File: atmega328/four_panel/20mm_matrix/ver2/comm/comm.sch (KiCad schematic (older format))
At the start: 11 parts, among them IC5 ATMEGA328-A, P1 CONN15, P2 CONN15, P4 CONN_2X2, P5 CONN_2X2, P6 CONN_2X2, P7 CONN_2X2, X5 CER_RESO

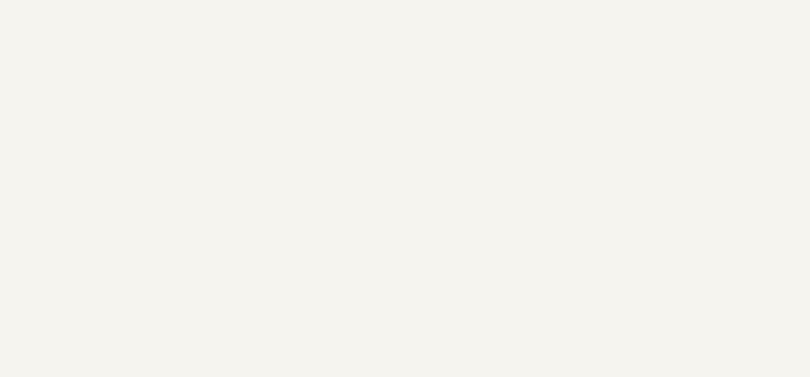
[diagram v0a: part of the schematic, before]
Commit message: Added ground pin header to backside of ver 2 com pcb.
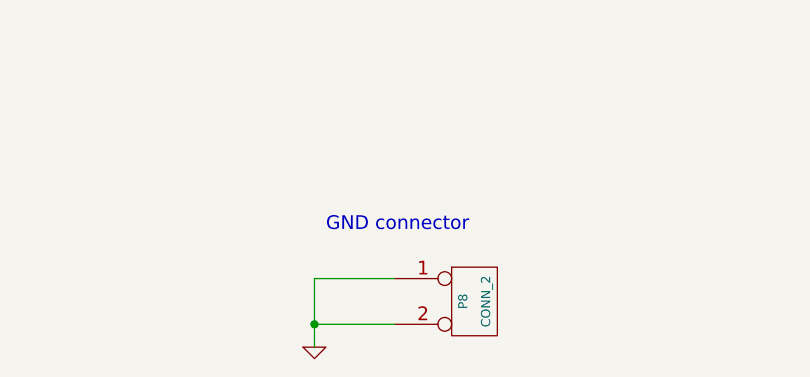
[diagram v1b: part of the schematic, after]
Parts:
- added P8: CONN_2, symbol CONN_2
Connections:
- net GND: now also P8.1 (P1), P8.2 (PM)
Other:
- note added: "GND connector"
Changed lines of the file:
@@
 NoConn ~ 14650 1650
 NoConn ~ 14650 2500
+$Comp
+L CONN_2 P8
+U 1 1 53C45937
+P 13050 5950
+F 0 "P8" V 13000 5950 40  0000 C CNN
+F 1 "CONN_2" V 13100 5950 40  0000 C CNN
+F 2 "" H 13050 5950 60  0000 C CNN
+F 3 "" H 13050 5950 60  0000 C CNN
+	1    13050 5950
+	1    0    0    -1
+$EndComp
+$Comp
+L GND #PWR019
+U 1 1 53C45946
+P 12350 6150
+F 0 "#PWR019" H 12350 6150 30  0001 C CNN
+F 1 "GND" H 12350 6080 30  0001 C CNN
+F 2 "" H 12350 6150 60  0000 C CNN
+F 3 "" H 12350 6150 60  0000 C CNN
+	1    12350 6150
+	1    0    0    -1
+$EndComp
+Wire Wire Line
+	12350 5850 12350 6150
+Wire Wire Line
+	12350 6050 12700 6050
+Wire Wire Line
+	12700 5850 12350 5850
+Connection ~ 12350 6050
+Text Notes 12400 5650 0    60   ~ 0
+GND connector
 $EndSCHEMATC

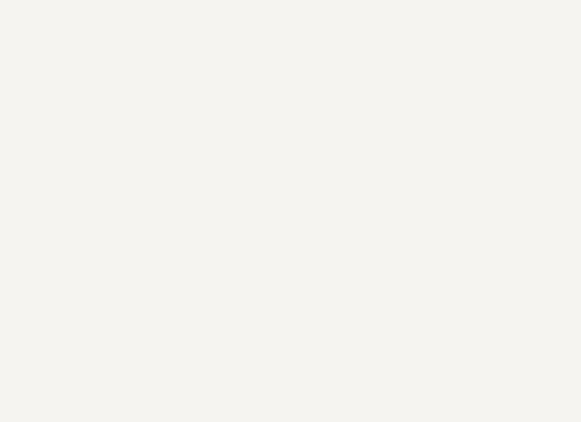
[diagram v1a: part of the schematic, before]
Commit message: Adde ground holes to 4x20mm atmega328 comm
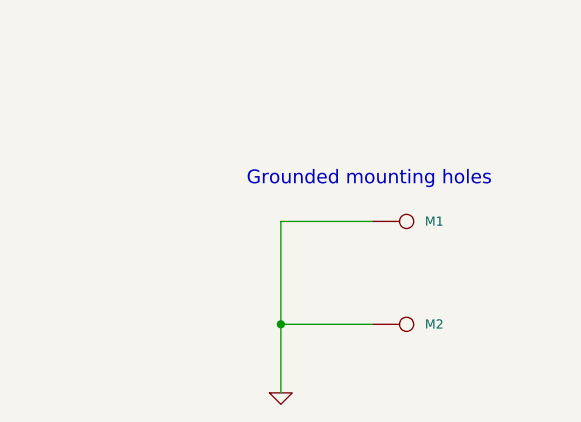
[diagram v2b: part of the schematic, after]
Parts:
- added M1, M2: CONN_1, symbol CONN_1
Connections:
- net GND: now also M1.1, M2.1
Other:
- note added: "Grounded mounting holes"
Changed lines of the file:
@@
 Text Notes 12400 5650 0    60   ~ 0
 GND connector
+$Comp
+L CONN_1 M1
+U 1 1 53CF2CE7
+P 15800 5650
+F 0 "M1" H 15880 5650 40  0000 L CNN
+F 1 "CONN_1" H 15800 5705 30  0001 C CNN
+F 2 "" H 15800 5650 60  0000 C CNN
+F 3 "" H 15800 5650 60  0000 C CNN
+	1    15800 5650
+	1    0    0    -1
+$EndComp
+$Comp
+L CONN_1 M2
+U 1 1 53CF2CF6
+P 15800 6100
+F 0 "M2" H 15880 6100 40  0000 L CNN
+F 1 "CONN_1" H 15800 6155 30  0001 C CNN
+F 2 "" H 15800 6100 60  0000 C CNN
+F 3 "" H 15800 6100 60  0000 C CNN
+	1    15800 6100
+	1    0    0    -1
+$EndComp
+Wire Wire Line
+	15650 5650 15250 5650
+Wire Wire Line
+	15250 5650 15250 6400
+Wire Wire Line
+	15250 6100 15650 6100
+Connection ~ 15250 6100
+$Comp
+L GND #PWR?
+U 1 1 53CF2DD9
+P 15250 6400
+F 0 "#PWR?" H 15250 6400 30  0001 C CNN
+F 1 "GND" H 15250 6330 30  0001 C CNN
+F 2 "" H 15250 6400 60  0000 C CNN
+F 3 "" H 15250 6400 60  0000 C CNN
+	1    15250 6400
+	1    0    0    -1
+$EndComp
+Text Notes 15100 5500 0    60   ~ 0
+Grounded mounting holes
 $EndSCHEMATC

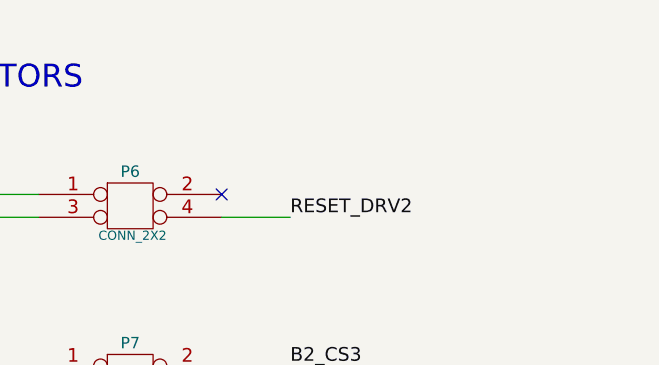
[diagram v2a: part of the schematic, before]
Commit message: Modified header on comm pcb.
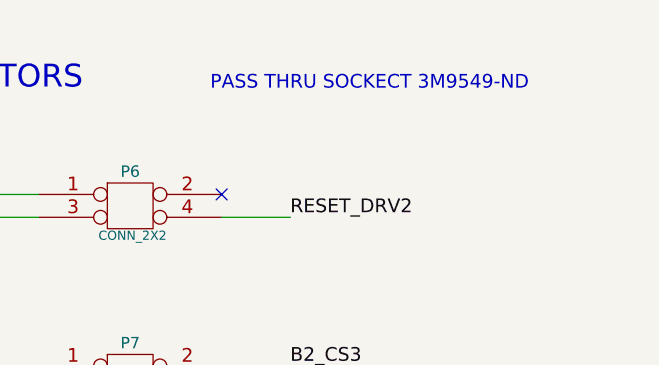
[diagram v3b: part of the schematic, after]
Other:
- note added: "PASS THRU SOCKECT 3M9549-ND"
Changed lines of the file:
@@
 Text Notes 15100 5500 0    60   ~ 0
 Grounded mounting holes
+Text Notes 14600 1200 0    60   ~ 0
+PASS THRU SOCKECT 3M9549-ND
 $EndSCHEMATC

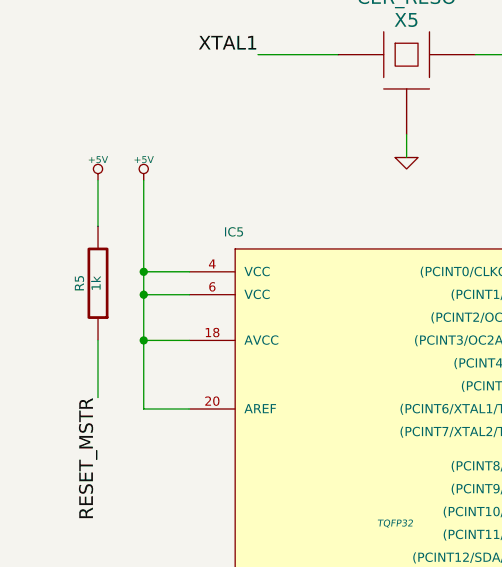
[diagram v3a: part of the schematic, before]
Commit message: Modified BOM for both comm and driver PCBs.
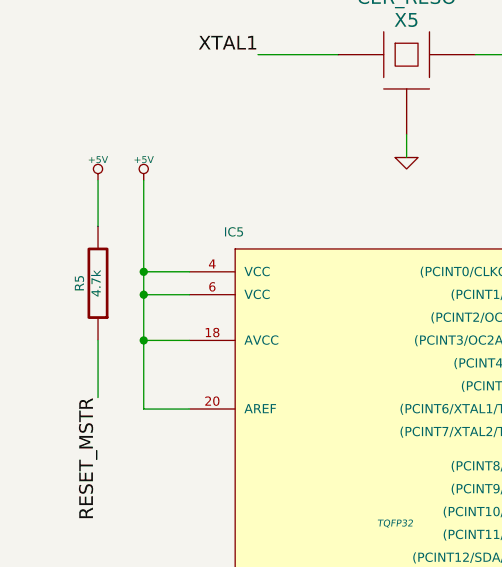
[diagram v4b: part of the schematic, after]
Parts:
- R5: value 1k -> 4.7k
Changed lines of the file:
@@
 P 1300 2450
 F 0 "R5" V 1380 2450 40  0000 C CNN
-F 1 "1k" V 1307 2451 40  0000 C CNN
+F 1 "4.7k" V 1307 2451 40  0000 C CNN
 F 2 "" V 1230 2450 30  0000 C CNN
 F 3 "" H 1300 2450 30  0000 C CNN

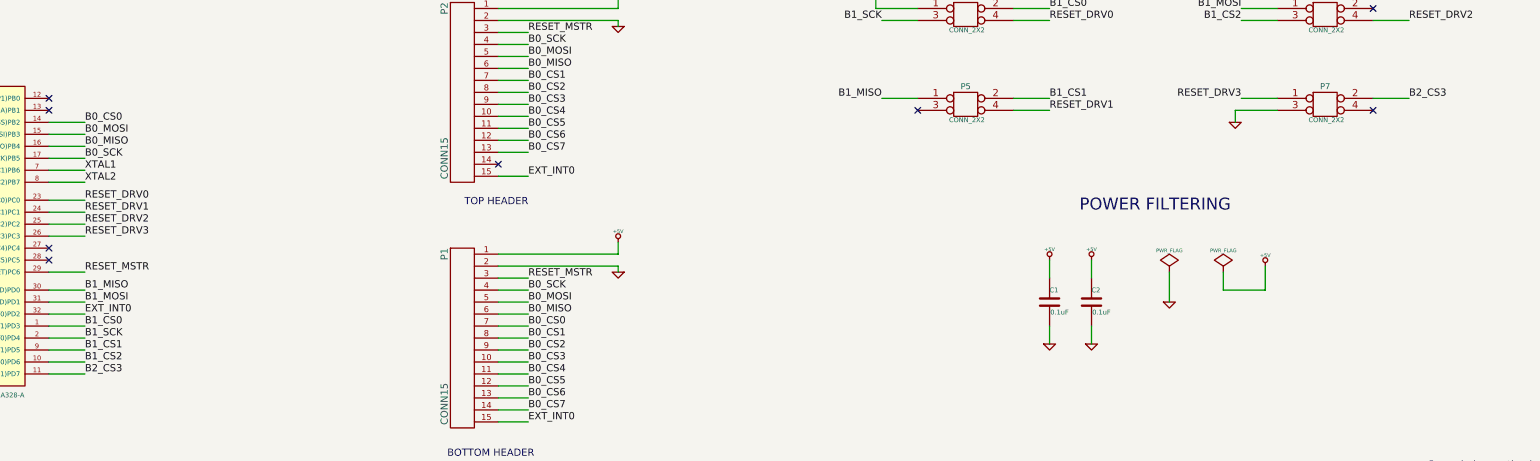
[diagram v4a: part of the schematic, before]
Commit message: Made new gerber files for 4x20mm comm sub-panel.
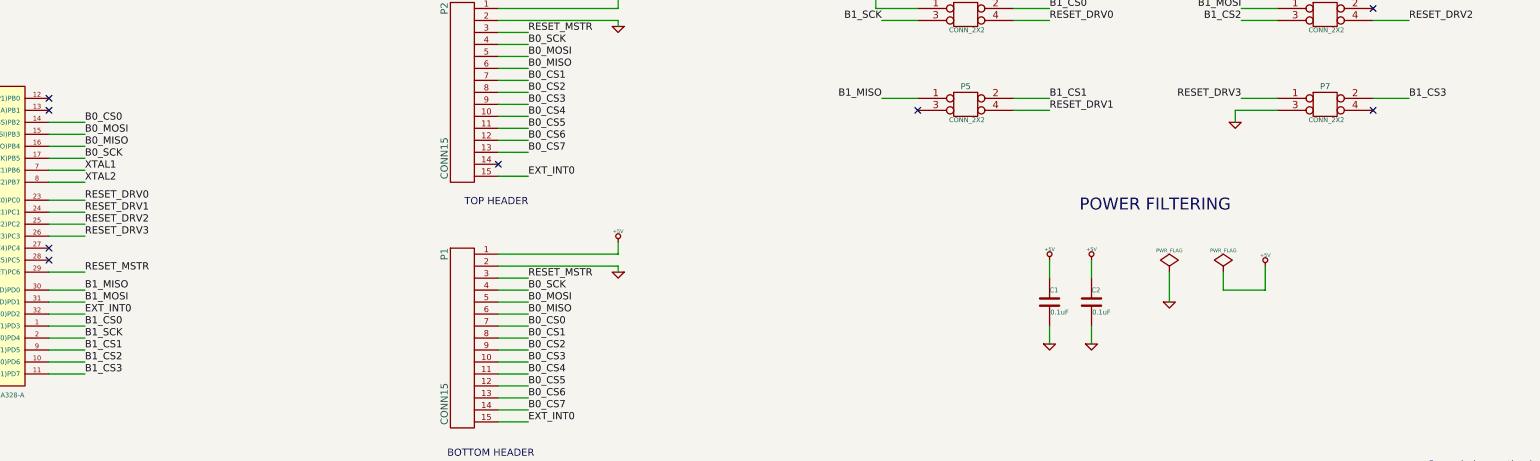
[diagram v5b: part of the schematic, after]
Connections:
- net B2_CS3 renamed B1_CS3
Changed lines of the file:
@@
 B1_CS2
 Text Label 3900 4700 0    60   ~ 0
-B2_CS3
+B1_CS3
 Wire Wire Line
 	10850 2400 10550 2400
@@
 B1_CS2
 Text Label 14950 2400 0    60   ~ 0
-B2_CS3
+B1_CS3
 Text Label 11950 1750 0    60   ~ 0
 RESET_DRV0
